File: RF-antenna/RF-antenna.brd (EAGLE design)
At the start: 108.2 x 108.2 mm, 52 parts, among them CON1 UMC_CONNECTORREGULAR, CON2 UMC_CONNECTORREGULAR, CON3 UMC_CONNECTORREGULAR, CON4 UMC_CONNECTORREGULAR, CON5 UMC_CONNECTORREGULAR, CON6 UMC_CONNECTORREGULAR, U1 THS3091DDAR, U2 THS3091DDAR, U3 THS3091DDAR, X1 SMA-V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

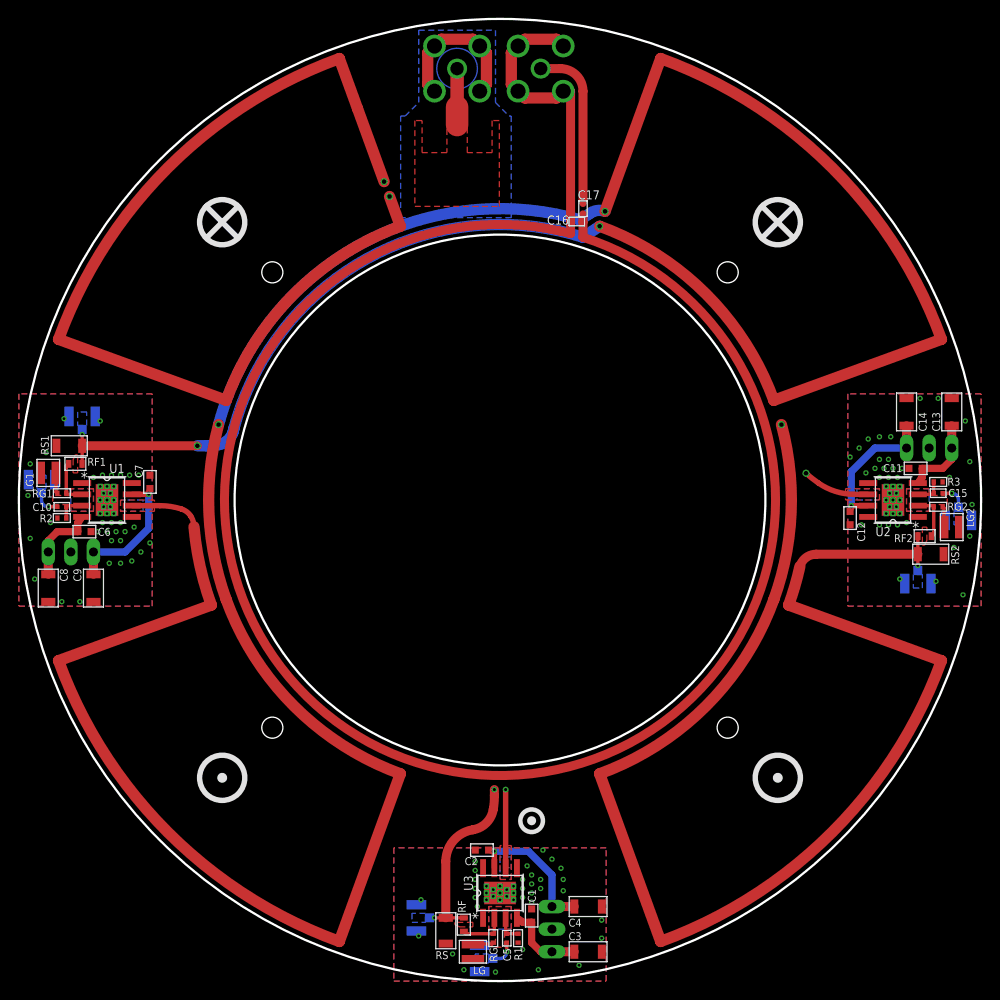
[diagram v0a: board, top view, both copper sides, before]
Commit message: Success
Got COMSOL to push, now updating with additional COMSOL and files for Macrofab.

DSB
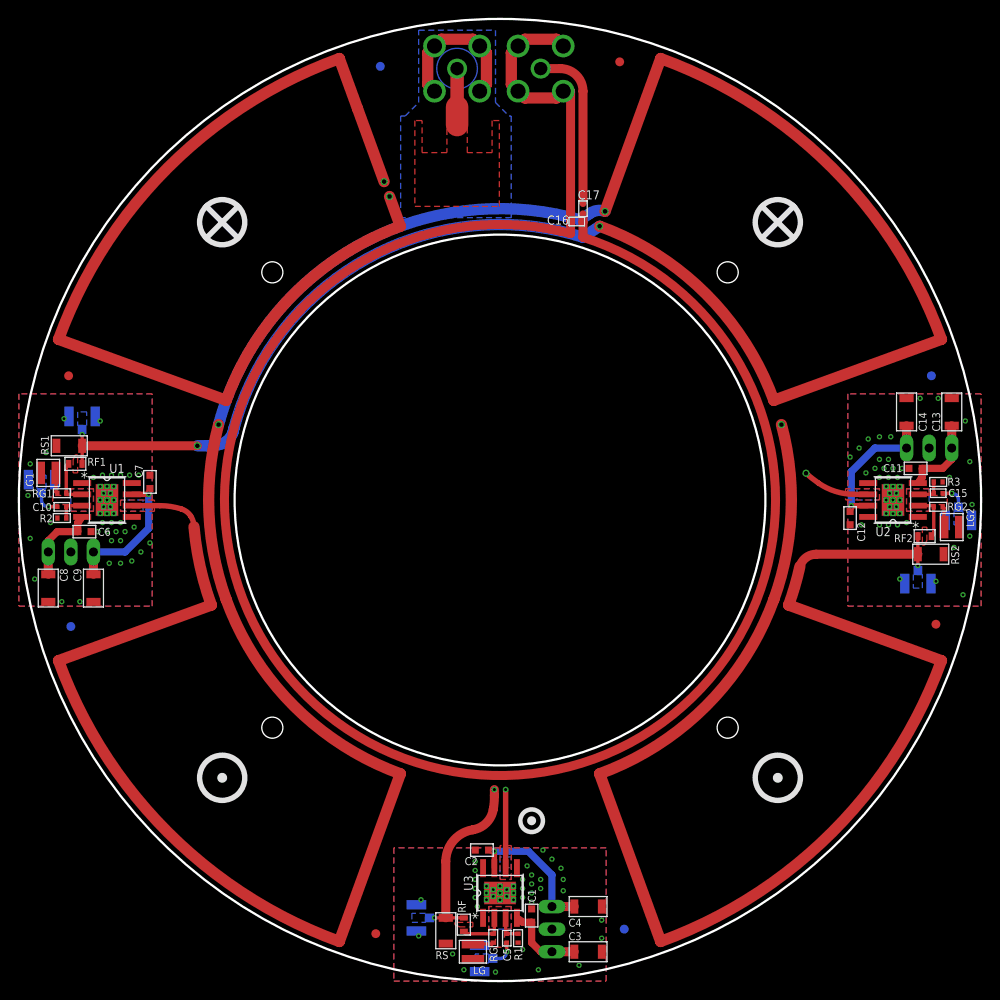
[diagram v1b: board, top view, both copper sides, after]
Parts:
- added FID1, FID2, FID3, FID4, FID5, FID6, FID7, FID8: FIDUCIAL-1.0MM, fiducials-jqi:FID_1.0MM
- JP1, JP2, JP3, LG, LG1, LG2: value (none) -> DNP
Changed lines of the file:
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@@
 <attribute name="PARTNO" value="PHP01206E10R0BST5" x="48.006" y="5.6642" size="1.778" layer="27" rot="R90" display="off"/>
 </element>
-<element name="JP1" library="pinhead" package="1X03" value="" x="59.944" y="5.842" smashed="yes" rot="MR90">
+<element name="JP1" library="pinhead" package="1X03" value="DNP" x="59.944" y="5.842" smashed="yes" rot="MR90">
 <attribute name="NAME" x="63.0428" y="1.9558" size="1.27" layer="26" ratio="10" rot="MR90"/>
 <attribute name="PARTNO" value="640456-3" x="59.944" y="5.842" size="1.778" layer="28" rot="MR90" display="off"/>
@@
 <attribute name="PARTNO" value="1909763-1" x="44.704" y="7.112" size="1.778" layer="28" rot="MR180" display="off"/>
 </element>
-<element name="LG" library="jqi_passives" package="1008" value="" x="51.054" y="3.302" smashed="yes">
+<element name="LG" library="jqi_passives" package="1008" value="DNP" x="51.054" y="3.302" smashed="yes">
 <attribute name="NAME" x="51.054" y="0.762" size="0.889" layer="25"/>
 <attribute name="VALUE" x="53.34" y="2.286" size="1.27" layer="27"/>
@@
 <attribute name="PARTNO" value="PHP01206E10R0BST5" x="5.6642" y="60.198" size="1.778" layer="27" display="off"/>
 </element>
-<element name="JP2" library="pinhead" package="1X03" value="" x="5.842" y="48.26" smashed="yes" rot="MR180">
+<element name="JP2" library="pinhead" package="1X03" value="DNP" x="5.842" y="48.26" smashed="yes" rot="MR180">
 <attribute name="NAME" x="1.9558" y="45.1612" size="1.27" layer="26" ratio="10" rot="MR180"/>
 <attribute name="PARTNO" value="640456-3" x="5.842" y="48.26" size="1.778" layer="28" rot="MR180" display="off"/>
@@
 <attribute name="PARTNO" value="1909763-1" x="7.112" y="63.5" size="1.778" layer="28" rot="MR270" display="off"/>
 </element>
-<element name="LG1" library="jqi_passives" package="1008" value="" x="3.302" y="57.15" smashed="yes" rot="R270">
+<element name="LG1" library="jqi_passives" package="1008" value="DNP" x="3.302" y="57.15" smashed="yes" rot="R270">
 <attribute name="NAME" x="0.762" y="57.15" size="0.889" layer="25" rot="R270"/>
 <attribute name="VALUE" x="2.286" y="54.864" size="1.27" layer="27" rot="R270"/>
@@
 <attribute name="PARTNO" value="PHP01206E10R0BST5" x="102.5398" y="48.006" size="1.778" layer="27" rot="R180" display="off"/>
 </element>
-<element name="JP3" library="pinhead" package="1X03" value="" x="102.362" y="59.944" smashed="yes" rot="MR0">
+<element name="JP3" library="pinhead" package="1X03" value="DNP" x="102.362" y="59.944" smashed="yes" rot="MR0">
 <attribute name="NAME" x="106.2482" y="63.0428" size="1.27" layer="26" ratio="10" rot="MR0"/>
 <attribute name="PARTNO" value="640456-3" x="102.362" y="59.944" size="1.778" layer="28" rot="MR0" display="off"/>
@@
 <attribute name="PARTNO" value="1909763-1" x="101.092" y="44.704" size="1.778" layer="28" rot="MR90" display="off"/>
 </element>
-<element name="LG2" library="jqi_passives" package="1008" value="" x="104.902" y="51.054" smashed="yes" rot="R90">
+<element name="LG2" library="jqi_passives" package="1008" value="DNP" x="104.902" y="51.054" smashed="yes" rot="R90">
 <attribute name="NAME" x="107.442" y="51.054" size="0.889" layer="25" rot="R90"/>
 <attribute name="VALUE" x="105.918" y="53.34" size="1.27" layer="27" rot="R90"/>
@@
 <element name="LW5" library="RFantenna" package="LITZ_100MHZ" value="LITZ_TERM" x="95.504" y="54.737"/>
 <element name="LW6" library="RFantenna" package="LITZ_100MHZ" value="LITZ_TERM" x="101.092" y="48.006"/>
-<element name="X1" library="connector-jqi" package="SMA-V" value="SMA-V" x="49.276" y="102.616" rot="MR0"/>
-<element name="X2" library="connector-jqi" package="SMA-V" value="SMA-V" x="58.674" y="102.616" rot="MR0"/>
+<element name="X1" library="connector-jqi" package="SMA-V" value="SMA-V" x="49.276" y="102.616" rot="MR0">
+<attribute name="PARTNO" value="5-1814832-1" x="49.276" y="102.616" size="1.778" layer="28" rot="MR0" display="off"/>
+</element>
+<element name="X2" library="connector-jqi" package="SMA-V" value="SMA-V" x="58.674" y="102.616" rot="MR0">
+<attribute name="PARTNO" value="5-1814832-1" x="58.674" y="102.616" size="1.778" layer="28" rot="MR0" display="off"/>
+</element>
 <element name="C16" library="jqi_passives" package="C_MLCC_0402" value="3pF" x="62.738" y="85.4202" smashed="yes" rot="R180">
 <attribute name="NAME" x="61.86" y="86.0902" size="1.016" layer="25" font="vector" rot="R180"/>
@@
 <attribute name="PARTNO" value="500R07S0R3AV4T" x="63.4365" y="86.868" size="1.778" layer="27" rot="R270" display="off"/>
 </element>
+<element name="FID1" library="fiducials-jqi" package="FID_1.0MM" value="FIDUCIAL-1.0MM" x="5.588" y="68.072"/>
+<element name="FID2" library="fiducials-jqi" package="FID_1.0MM" value="FIDUCIAL-1.0MM" x="40.132" y="5.334"/>
+<element name="FID3" library="fiducials-jqi" package="FID_1.0MM" value="FIDUCIAL-1.0MM" x="103.124" y="40.132"/>
+<element name="FID4" library="fiducials-jqi" package="FID_1.0MM" value="FIDUCIAL-1.0MM" x="67.564" y="103.378"/>
+<element name="FID5" library="fiducials-jqi" package="FID_1.0MM" value="FIDUCIAL-1.0MM" x="68.072" y="5.842" rot="MR0"/>
+<element name="FID6" library="fiducials-jqi" package="FID_1.0MM" value="FIDUCIAL-1.0MM" x="40.64" y="102.87" rot="MR0"/>
+<element name="FID7" library="fiducials-jqi" package="FID_1.0MM" value="FIDUCIAL-1.0MM" x="5.842" y="39.878" rot="MR0"/>
+<element name="FID8" library="fiducials-jqi" package="FID_1.0MM" value="FIDUCIAL-1.0MM" x="102.616" y="68.072" rot="MR0"/>
 </elements>
 <signals>

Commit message: New 87Rb and 6Li antennas
I updated the eagle files with the new 87Rb and 6Li antenna designs from COMSOL.

DSB
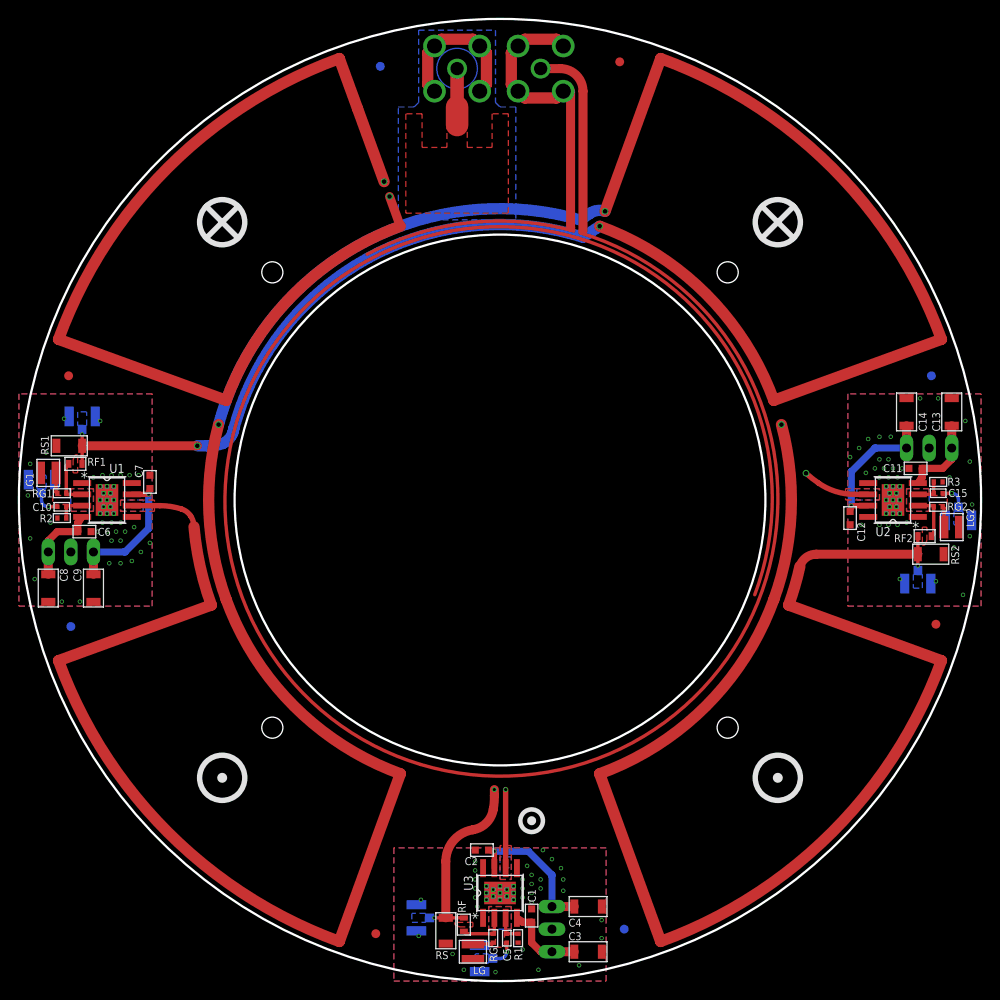
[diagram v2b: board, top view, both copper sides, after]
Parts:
- removed C16: 3pF, jqi_passives:C_MLCC_0402
- removed C17: 0.3pF, jqi_passives:C_MLCC_0402
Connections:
- net COIL6LI_N: no longer C16.P$1, C16.P$2, C17.P$2
- net COIL6LI_P: no longer C17.P$1
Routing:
- net COIL6LI_P: track 18.5 -> 191.1 mm
- net COIL6LI_N: track 41.3 -> 57.4 mm

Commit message: Updated values
Changed values in BOM to reflect results from prototype antennas.

DSB
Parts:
- RF: value 866 -> 220
- RF1, RF2: value 866 -> 422
- RG: value 95.3 -> 24.3
- RG1, RG2: value 95.3 -> 46.4
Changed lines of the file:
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@@
 <element name="C3" library="jqi_passives" package="C_MLCC_1206" value="10uF" x="64.008" y="3.302" smashed="yes">
 <attribute name="NAME" x="61.808" y="4.602" size="0.889" layer="25" font="vector"/>
-<attribute name="PARTNO" value="C3216X5R1H106K160AB" x="64.008" y="3.302" size="1.778" layer="27" display="off"/>
+<attribute name="PARTNO" value="CL31A106MBHNNNE" x="64.008" y="3.302" size="1.778" layer="27" display="off"/>
 </element>
 <element name="C4" library="jqi_passives" package="C_MLCC_1206" value="10uF" x="64.008" y="8.382" smashed="yes">
 <attribute name="NAME" x="61.808" y="6.126" size="0.889" layer="25" font="vector"/>
-<attribute name="PARTNO" value="C3216X5R1H106K160AB" x="64.008" y="8.382" size="1.778" layer="27" display="off"/>
+<attribute name="PARTNO" value="CL31A106MBHNNNE" x="64.008" y="8.382" size="1.778" layer="27" display="off"/>
 </element>
 <element name="CON2" library="qkdlab_alessandro" package="UMC_CONNECTOR" value="UMC_CONNECTORREGULAR" x="51.816" y="2.54" smashed="yes" rot="MR180">
@@
 <attribute name="PARTNO" value="ERA-2AEB49R9X" x="56.134" y="4.826" size="1.778" layer="27" rot="R90" display="off"/>
 </element>
-<element name="RG" library="jqi_passives" package="R_0402" value="95.3" x="53.34" y="4.826" smashed="yes" rot="R270">
+<element name="RG" library="jqi_passives" package="R_0402" value="24.3" x="53.34" y="4.826" smashed="yes" rot="R270">
 <attribute name="NAME" x="52.924" y="3.794" size="0.889" layer="25" font="vector" ratio="10" rot="R270"/>
-<attribute name="PARTNO" value="ERA-2AEB95R3X" x="53.34" y="4.826" size="1.778" layer="27" rot="R270" display="off"/>
+<attribute name="PARTNO" value="RP73PF1E24R3BTD" x="53.34" y="4.826" size="1.778" layer="27" rot="R270" display="off"/>
 </element>
-<element name="RF" library="jqi_passives" package="R_0603" value="866" x="50.038" y="6.35" smashed="yes" rot="R90">
+<element name="RF" library="jqi_passives" package="R_0603" value="220" x="50.038" y="6.35" smashed="yes" rot="R90">
 <attribute name="NAME" x="50.254" y="7.69" size="0.889" layer="25" font="vector" rot="R90"/>
-<attribute name="PARTNO" value="ERA-3AEB8660V" x="50.038" y="6.35" size="1.778" layer="27" rot="R90" display="off"/>
+<attribute name="PARTNO" value="TNPW0603220RBEEA" x="50.038" y="6.35" size="1.778" layer="27" rot="R90" display="off"/>
 </element>
 <element name="C5" library="jqi_passives" package="C_MLCC_0402" value="10nF" x="54.864" y="4.826" smashed="yes" rot="R90">
@@
 <element name="C8" library="jqi_passives" package="C_MLCC_1206" value="10uF" x="3.302" y="44.196" smashed="yes" rot="R270">
 <attribute name="NAME" x="4.602" y="46.396" size="0.889" layer="25" font="vector" rot="R270"/>
-<attribute name="PARTNO" value="C3216X5R1H106K160AB" x="3.302" y="44.196" size="1.778" layer="27" rot="R270" display="off"/>
+<attribute name="PARTNO" value="CL31A106MBHNNNE" x="3.302" y="44.196" size="1.778" layer="27" rot="R270" display="off"/>
 </element>
 <element name="C9" library="jqi_passives" package="C_MLCC_1206" value="10uF" x="8.382" y="44.196" smashed="yes" rot="R270">
 <attribute name="NAME" x="6.126" y="46.396" size="0.889" layer="25" font="vector" rot="R270"/>
-<attribute name="PARTNO" value="C3216X5R1H106K160AB" x="8.382" y="44.196" size="1.778" layer="27" rot="R270" display="off"/>
+<attribute name="PARTNO" value="CL31A106MBHNNNE" x="8.382" y="44.196" size="1.778" layer="27" rot="R270" display="off"/>
 </element>
 <element name="CON3" library="qkdlab_alessandro" package="UMC_CONNECTOR" value="UMC_CONNECTORREGULAR" x="2.54" y="56.388" smashed="yes" rot="MR270">
@@
 <attribute name="PARTNO" value="ERA-2AEB49R9X" x="4.826" y="52.07" size="1.778" layer="27" display="off"/>
 </element>
-<element name="RG1" library="jqi_passives" package="R_0402" value="95.3" x="4.826" y="54.864" smashed="yes" rot="R180">
+<element name="RG1" library="jqi_passives" package="R_0402" value="46.4" x="4.826" y="54.864" smashed="yes" rot="R180">
 <attribute name="NAME" x="3.794" y="55.28" size="0.889" layer="25" font="vector" ratio="10" rot="R180"/>
-<attribute name="PARTNO" value="ERA-2AEB95R3X" x="4.826" y="54.864" size="1.778" layer="27" rot="R180" display="off"/>
+<attribute name="PARTNO" value="RP73PF1E46R4BTD" x="4.826" y="54.864" size="1.778" layer="27" rot="R180" display="off"/>
 </element>
-<element name="RF1" library="jqi_passives" package="R_0603" value="866" x="6.35" y="58.166" smashed="yes">
+<element name="RF1" library="jqi_passives" package="R_0603" value="422" x="6.35" y="58.166" smashed="yes">
 <attribute name="NAME" x="7.69" y="57.95" size="0.889" layer="25" font="vector"/>
-<attribute name="PARTNO" value="ERA-3AEB8660V" x="6.35" y="58.166" size="1.778" layer="27" display="off"/>
+<attribute name="PARTNO" value="TNPW0603422RBEEA" x="6.35" y="58.166" size="1.778" layer="27" display="off"/>
 </element>
 <element name="C10" library="jqi_passives" package="C_MLCC_0402" value="10nF" x="4.826" y="53.34" smashed="yes">
@@
 <element name="C13" library="jqi_passives" package="C_MLCC_1206" value="10uF" x="104.902" y="64.008" smashed="yes" rot="R90">
 <attribute name="NAME" x="103.602" y="61.808" size="0.889" layer="25" font="vector" rot="R90"/>
-<attribute name="PARTNO" value="C3216X5R1H106K160AB" x="104.902" y="64.008" size="1.778" layer="27" rot="R90" display="off"/>
+<attribute name="PARTNO" value="CL31A106MBHNNNE" x="104.902" y="64.008" size="1.778" layer="27" rot="R90" display="off"/>
 </element>
 <element name="C14" library="jqi_passives" package="C_MLCC_1206" value="10uF" x="99.822" y="64.008" smashed="yes" rot="R90">
 <attribute name="NAME" x="102.078" y="61.808" size="0.889" layer="25" font="vector" rot="R90"/>
-<attribute name="PARTNO" value="C3216X5R1H106K160AB" x="99.822" y="64.008" size="1.778" layer="27" rot="R90" display="off"/>
+<attribute name="PARTNO" value="CL31A106MBHNNNE" x="99.822" y="64.008" size="1.778" layer="27" rot="R90" display="off"/>
 </element>
 <element name="CON5" library="qkdlab_alessandro" package="UMC_CONNECTOR" value="UMC_CONNECTORREGULAR" x="105.664" y="51.816" smashed="yes" rot="MR90">
@@
 <attribute name="PARTNO" value="ERA-2AEB49R9X" x="103.378" y="56.134" size="1.778" layer="27" rot="R180" display="off"/>
 </element>
-<element name="RG2" library="jqi_passives" package="R_0402" value="95.3" x="103.378" y="53.34" smashed="yes">
+<element name="RG2" library="jqi_passives" package="R_0402" value="46.4" x="103.378" y="53.34" smashed="yes">
 <attribute name="NAME" x="104.41" y="52.924" size="0.889" layer="25" font="vector" ratio="10"/>
-<attribute name="PARTNO" value="ERA-2AEB95R3X" x="103.378" y="53.34" size="1.778" layer="27" display="off"/>
+<attribute name="PARTNO" value="RP73PF1E46R4BTD" x="103.378" y="53.34" size="1.778" layer="27" display="off"/>
 </element>
-<element name="RF2" library="jqi_passives" package="R_0603" value="866" x="101.854" y="50.038" smashed="yes" rot="R180">
+<element name="RF2" library="jqi_passives" package="R_0603" value="422" x="101.854" y="50.038" smashed="yes" rot="R180">
 <attribute name="NAME" x="100.514" y="50.254" size="0.889" layer="25" font="vector" rot="R180"/>
-<attribute name="PARTNO" value="ERA-3AEB8660V" x="101.854" y="50.038" size="1.778" layer="27" rot="R180" display="off"/>
+<attribute name="PARTNO" value="TNPW0603422RBEEA" x="101.854" y="50.038" size="1.778" layer="27" rot="R180" display="off"/>
 </element>
 <element name="C15" library="jqi_passives" package="C_MLCC_0402" value="10nF" x="103.378" y="54.864" smashed="yes" rot="R180">
